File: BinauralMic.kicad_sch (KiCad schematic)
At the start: 25 parts, among them IC1 PCM2903CDBR, J1 156-4218-E, SW1 SW_Push, SW2 SW_Push, SW3 SW_Push, U1 74LVC1G08, U2 MIC5504-3.3YM5, X1 ECS-120-8-36-CKM-TR3

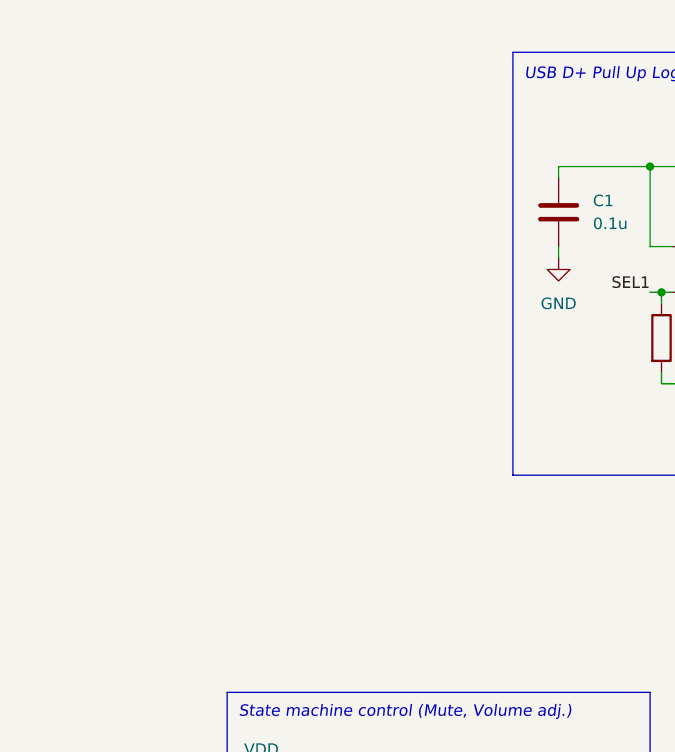
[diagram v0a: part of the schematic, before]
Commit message: Add USB port
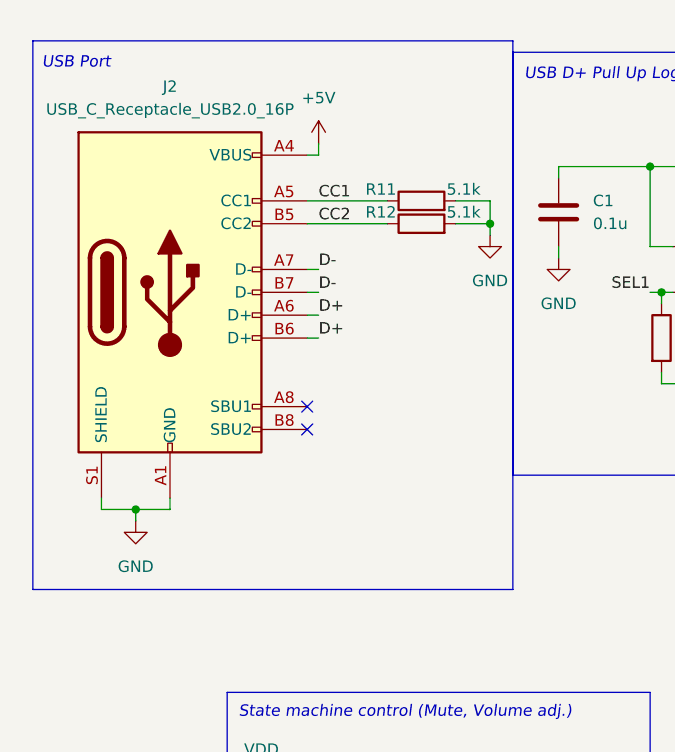
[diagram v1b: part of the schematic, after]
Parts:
- added J2: USB_C_Receptacle_USB2.0_16P, Connector_USB:USB_C_Receptacle_GCT_USB4105-xx-A_16P_TopMnt_Horizontal, symbol Connector:USB_C_Receptacle_USB2.0_16P
- added R11, R12: 5.1k, symbol Device:R
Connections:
- net +5V: now also J2.A4 (VBUS), J2.A9 (VBUS), J2.B4 (VBUS), J2.B9 (VBUS)
- net D+: now also J2.A6 (D+), J2.B6 (D+)
- net D-: now also J2.A7 (D-), J2.B7 (D-)
- net GND: now also J2.A1 (GND), J2.A12 (GND), J2.B1 (GND), J2.B12 (GND), J2.S1 (SHIELD), R11.2, R12.2
- new net CC1: J2.A5 (CC1), R11.1
- new net CC2: J2.B5 (CC2), R12.1
- no-connect marks 2 -> 4
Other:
- note added: "USB Port"

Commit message: Organization
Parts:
- added J3, J4: Conn_01x02_Pin, Connector_PinHeader_2.00mm:PinHeader_1x02_P2.00mm_Vertical, symbol Connector:Conn_01x02_Pin
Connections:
- net SEL1 is gone; now on net VBUS: IC1.9 (SEL1), R8.1, U1.2
- net VCOM: now also J3.2 (Pin_2), J4.2 (Pin_2)
- net VIN_{L}: now also J3.1 (Pin_1)
- net VIN_{R}: now also J4.1 (Pin_1)
- net DOUT_R: now reaches J1.1 (In1), R3.2
- net DIN_R: now reaches J1.3 (In2), R9.2
- net +5V renamed VBUS
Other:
- note added: "Microphone inputs"
- moved on the sheet: C1, C2, C3, C4, C5, C6, C7, IC1, J1A, J1B, J2, R1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

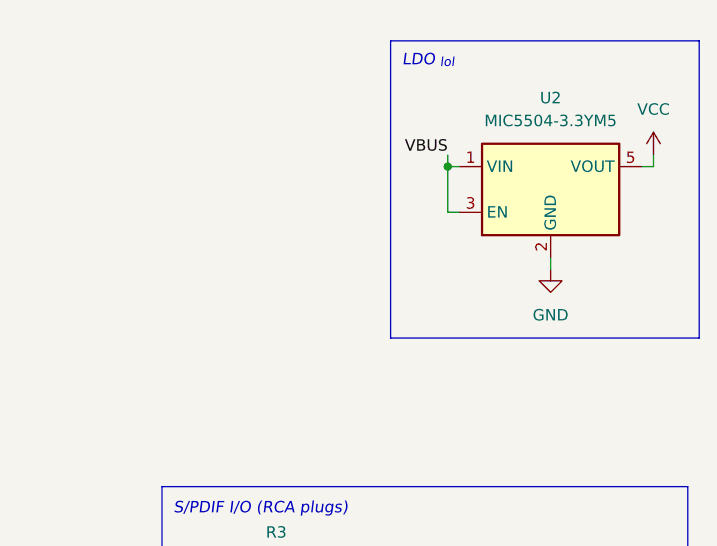
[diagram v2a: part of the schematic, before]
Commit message: Added input filter
LTSpice simulation to come soon
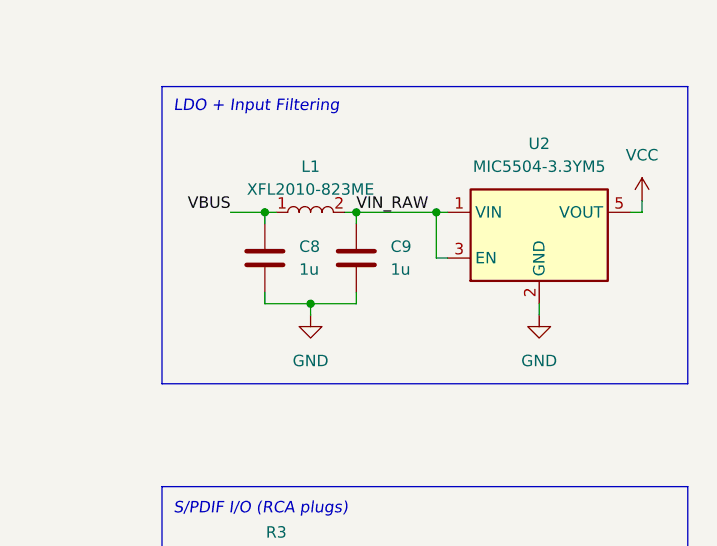
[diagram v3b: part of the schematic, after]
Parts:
- added C8, C9: 1u, symbol Device:C
- added L1: XFL2010-823ME, Inductor_SMD:L_Coilcraft_XFL2010, symbol Device:L
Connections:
- net GND: now also C8.2, C9.2
- net VBUS: now also C8.1, L1.1; no longer U2.1 (VIN), U2.3 (EN)
- new net VIN_RAW: C9.1, L1.2, U2.1 (VIN), U2.3 (EN)
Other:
- note added: "LDO + Input Filtering"
- note removed: "LDO _{lol}"
- moved on the sheet: U2

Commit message: Add various things
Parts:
- added C10: 22u, symbol Device:C
- added D1: LED, LED_SMD:LED_0603_1608Metric_Pad1.05x0.95mm_HandSolder, symbol Device:LED
- added MK1, MK2: Microphone, symbol Device:Microphone
- added R13: 5.6k, symbol Device:R
- C8: value 1u -> 22u
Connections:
- net GND: now also C10.2
- net VCOM: now also MK1.1 (-), MK2.1 (-)
- net VDD: now also D1.2 (A)
- net VIN_RAW: now also C10.1
- net VIN_{L}: now also MK1.2 (+)
- net VIN_{R}: now also MK2.2 (+)
- net ~{SSPND}: now also R13.2
- new net: D1.1 (K), R13.1
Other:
- moved on the sheet: C8, C9, L1, U2

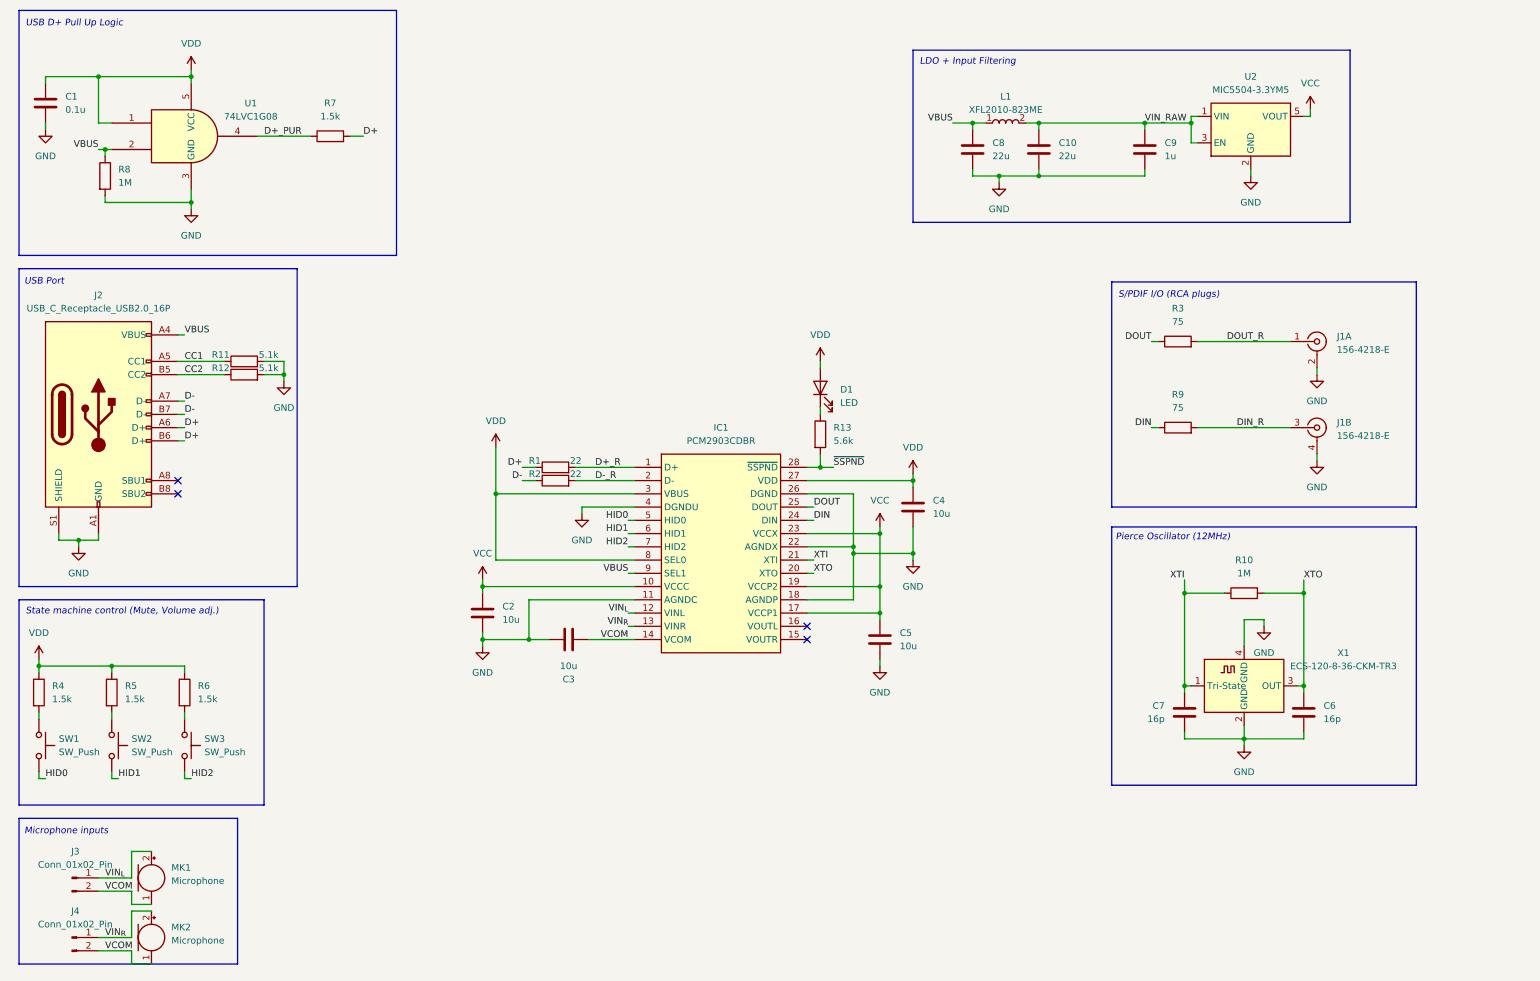
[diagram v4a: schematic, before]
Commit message: Add simulations and new op amp preamp
And hand calcs
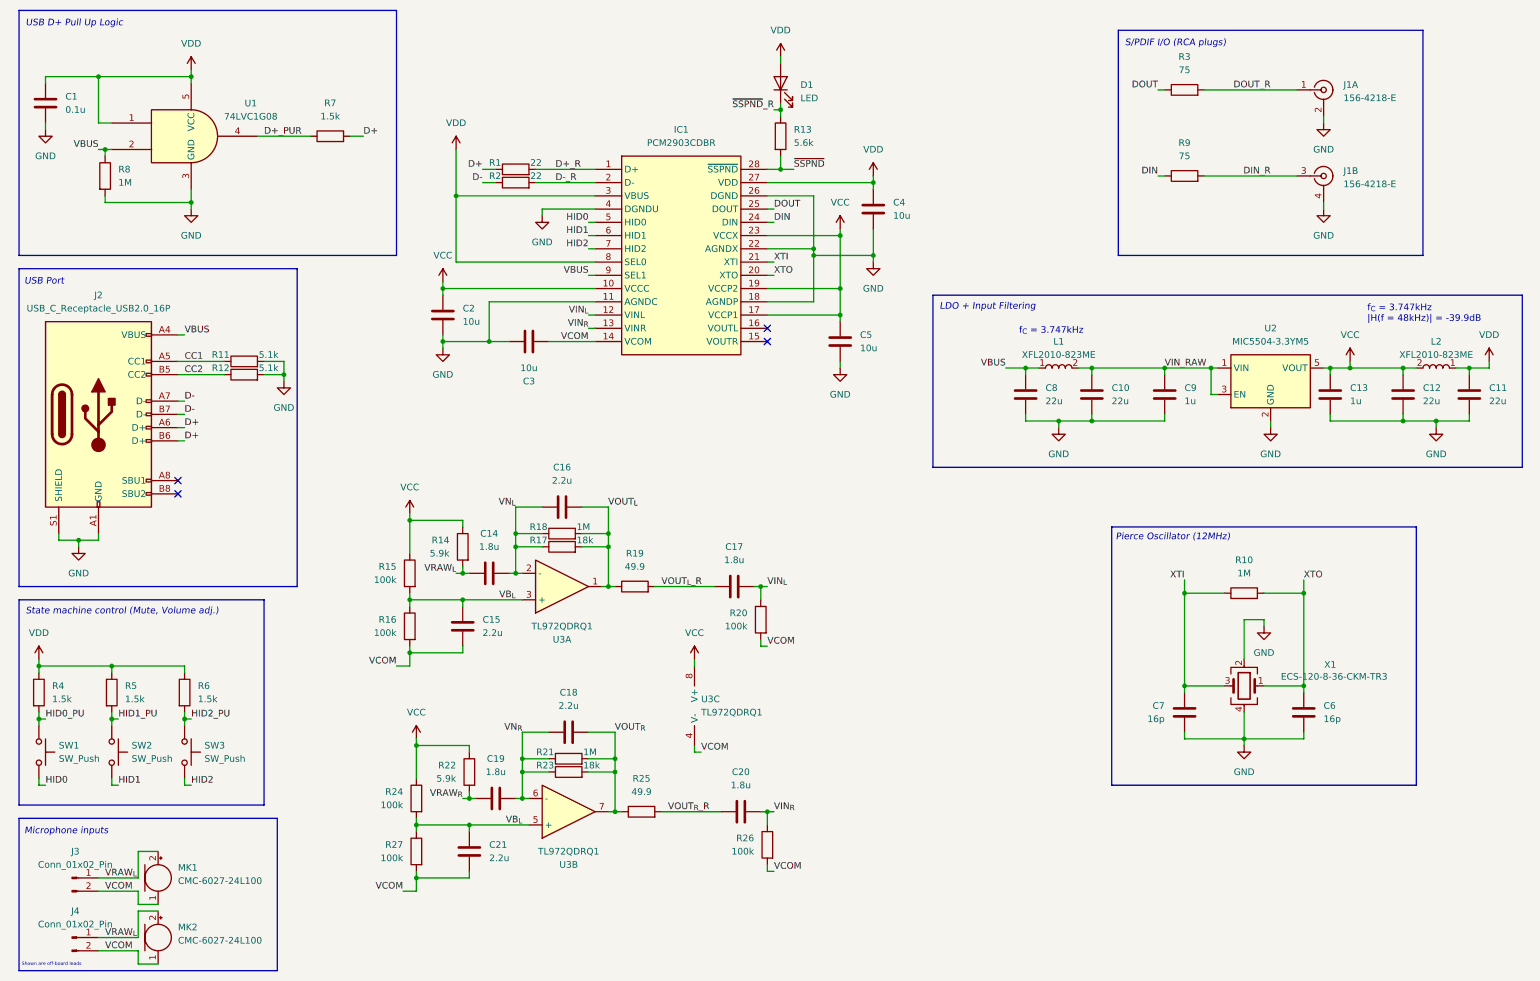
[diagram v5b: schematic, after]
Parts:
- added C11, C12: 22u, symbol Device:C
- added C13: 1u, symbol Device:C
- added C14, C17, C19, C20: 1.8u, Capacitor_SMD:C_0603_1608Metric_Pad1.08x0.95mm_HandSolder, symbol Device:C
- added C15, C16, C18, C21: 2.2u, Capacitor_SMD:C_0603_1608Metric_Pad1.08x0.95mm_HandSolder, symbol Device:C
- added L2: XFL2010-823ME, Inductor_SMD:L_Coilcraft_XFL2010, symbol Device:L
- added R14, R22: 5.9k, symbol Device:R
- added R15, R16, R20, R24, R26, R27: 100k, symbol Device:R
- added R17, R23: 18k, symbol Device:R
- added R18, R21: 1M, symbol Device:R
- added R19, R25: 49.9, symbol Device:R
- added U3: TL972QDRQ1, Package_SO:SOIC-8_3.9x4.9mm_P1.27mm, symbol Device:Opamp_Dual
- MK1, MK2: value Microphone -> CMC-6027-24L100; Mouser Part Number (none) -> 490-CMC-6027-24L100
- X1: symbol Oscillator:ECS-2520MV-xxx-xx -> Device:Crystal_GND24
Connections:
- net GND: now also C11.2, C12.2, C13.2
- net VCC: now also C12.1, C13.1, L2.2, R14.1, R15.1, R22.1, R24.1, U3.8 (V+)
- net VCOM: now also C15.1, C21.1, R16.2, R20.2, R26.2, R27.2, U3.4 (V-)
- net VDD: now also C11.1, L2.1
- net VIN_{L}: now also C17.2, R20.1; no longer J3.1 (Pin_1), MK1.2 (+)
- net VIN_{R}: now also C20.2, R26.1; no longer J4.1 (Pin_1), MK2.2 (+)
- net XTI: now also X1.3; no longer X1.1 (Tri-State)
- net XTO: now also X1.1; no longer X1.3 (OUT)
- net HID2_PU: now reaches R6.2, SW3.1
- net ~{SSPND}_R: now reaches D1.1 (K), R13.1
- net HID1_PU: now reaches R5.2, SW2.1
- net HID0_PU: now reaches R4.2, SW1.1
- new net VB_{L}: C15.2, C21.2, R15.2, R16.1, R24.2, R27.1, U3.3 (+), U3.5 (+)
- new net VN_{L}: C14.2, C16.1, R17.1, R18.1, U3.2 (-)
- new net VN_{R}: C18.1, C19.2, R21.1, R23.1, U3.6 (-)
- new net VOUT_{L}: C16.2, R17.2, R18.2, R19.1, U3.1
- new net VOUT_{L}_R: C17.1, R19.2
- new net VOUT_{R}: C18.2, R21.2, R23.2, R25.1, U3.7
- new net VOUT_{R}_R: C20.1, R25.2
- new net VRAW_{L}: C14.1, J3.1 (Pin_1), J4.1 (Pin_1), MK1.2 (+), MK2.2 (+), R14.2
- new net VRAW_{R}: C19.1, R22.2
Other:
- note added: "Shown are off-board leads"
- note added: "f_{C} = 3.747kHz"
- note added: "f_{C} = 3.747kHz |H(f = 48kHz)| = -39.9dB"
- moved on the sheet: C10, C2, C3, C4, C5, C8, C9, D1, IC1, J1A, J1B, L1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

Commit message: Copy the correct values from the hand calcs & copy to simulations
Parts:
- C14, C17, C19, C20: value 1.8u -> 4.7u
- C15, C21: value 2.2u -> 4.7u
- C16, C18: value 2.2u -> 68p
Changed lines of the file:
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@@
 			)
 		)
-		(property "Value" "2.2u"
+		(property "Value" "4.7u"
 			(at 101.6 132.0799 0)
 			(effects
@@
 			)
 		)
-		(property "Value" "1.8u"
+		(property "Value" "4.7u"
 			(at 104.14 158.75 90)
 			(effects
@@
 			)
 		)
-		(property "Value" "2.2u"
+		(property "Value" "68p"
 			(at 116.84 102.87 90)
 			(effects
@@
 			)
 		)
-		(property "Value" "1.8u"
+		(property "Value" "4.7u"
 			(at 102.87 115.57 90)
 			(effects
@@
 		(on_board yes)
 		(dnp no)
-		(fields_autoplaced yes)
 		(property "Reference" "C21"
 			(at 102.87 172.7199 0)
@@
 			)
 		)
-		(property "Value" "2.2u"
+		(property "Value" "4.7u"
 			(at 102.87 175.2599 0)
 			(effects
@@
 			)
 		)
-		(property "Value" "2.2u"
+		(property "Value" "68p"
 			(at 118.11 146.05 90)
 			(effects
@@
 			)
 		)
-		(property "Value" "1.8u"
+		(property "Value" "4.7u"
 			(at 149.86 118.11 90)
 			(effects
@@
 		(on_board yes)
 		(dnp no)
-		(fields_autoplaced yes)
 		(property "Reference" "C20"
 			(at 151.13 158.75 90)
@@
 			)
 		)
-		(property "Value" "1.8u"
+		(property "Value" "4.7u"
 			(at 151.13 161.29 90)
 			(effects
